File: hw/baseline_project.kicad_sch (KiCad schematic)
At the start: 20 parts, among them J101 EXT_3V3, Q101 IRLD024PBF, SW101 UP, SW102 DOWN, SW103 LEFT, SW104 RIGHT, SW105 MODE, U101 EK-TM4C123GXL, U102 ESP8266-1, U103 Adafruit ST7735R

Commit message: WIP hardware diagram
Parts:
- added D1: LED, ECE445L:LED_D5.0mm, symbol ECE 445L:LED
- added D2: 1N914, Diode_THT:D_DO-35_SOD27_P7.62mm_Horizontal, symbol Diode:1N914
- added LS1: Speaker, symbol Device:Speaker
- added Q1: IRLD024PBF, ECE445L:DIP920W60P254L490H457Q4N, symbol ECE 445L:IRLD024PBF
- added R1: 330, symbol Device:R_US
- added R2: 10K, symbol Device:R_US
- added R3: 0-2k, ECE445L:Potentiometer, symbol ECE 445L:Potentiometer
- added R4: 1k, symbol Device:R_US
- added R5: 10k, symbol Device:R_US
- added SW1, SW2, SW3, SW4, SW5: UP, ECE445L:SW_PUSH_6mm, symbol ECE 445L:SW_Push
- added U1: HiLetGo_ST7735R, ECE445L:hiletgo_st7735r, symbol ECE 445L:HiLetGo_ST7735R
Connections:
- net +3V3: now also D2.1 (K), LS1.1, R2.1, R4.1, U1.15 (LED+), U1.2 (VCC)
- net GND: now also D1.1 (K), Q1.4 (S), R3.3, SW1.1, U1.1 (GND), U1.16 (LED-)
- net PC6: now also R2.2, SW1.2
- net PE1: now also R3.1, R4.2
- net PE2: now also R1.1
- net PF1: now also R5.1
- new net: D2.2 (A), LS1.2, Q1.1 (D), Q1.2 (D)
- new net: Q1.3 (G), R5.2
- new net: D1.2 (A), R1.2
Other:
- note added: "Lab 1 Schematics"
- note added: "Lab 2 Schematics"
- note added: "Lab 3 Schematics"
- note added: "Negative Logic"
- note added: "Positive Logic"

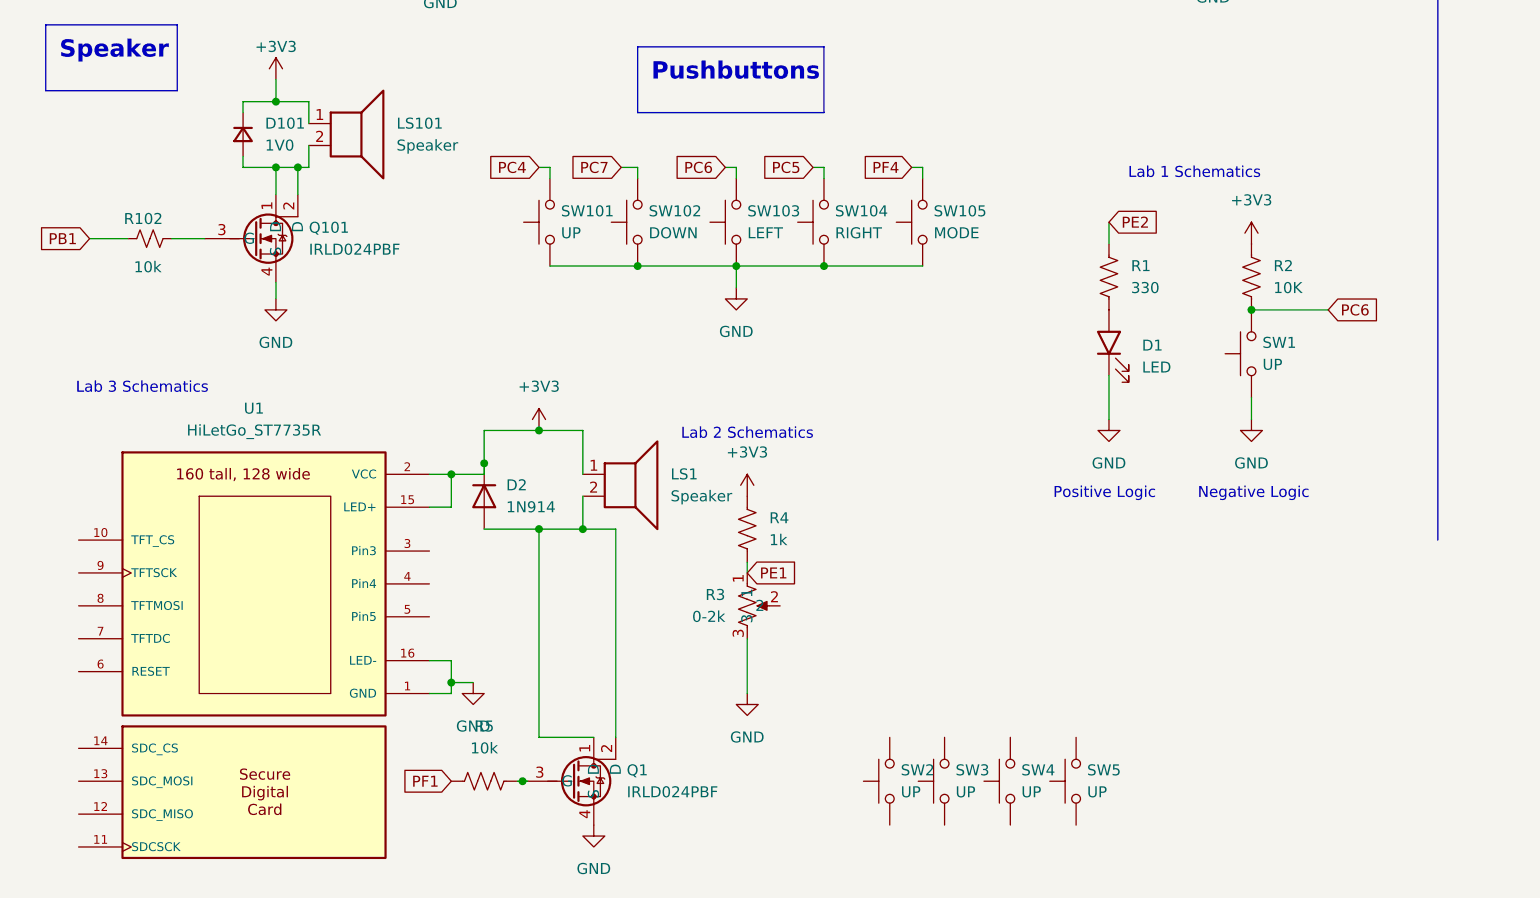
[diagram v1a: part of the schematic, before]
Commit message: HW done for current specs, completed some of prep deliverables
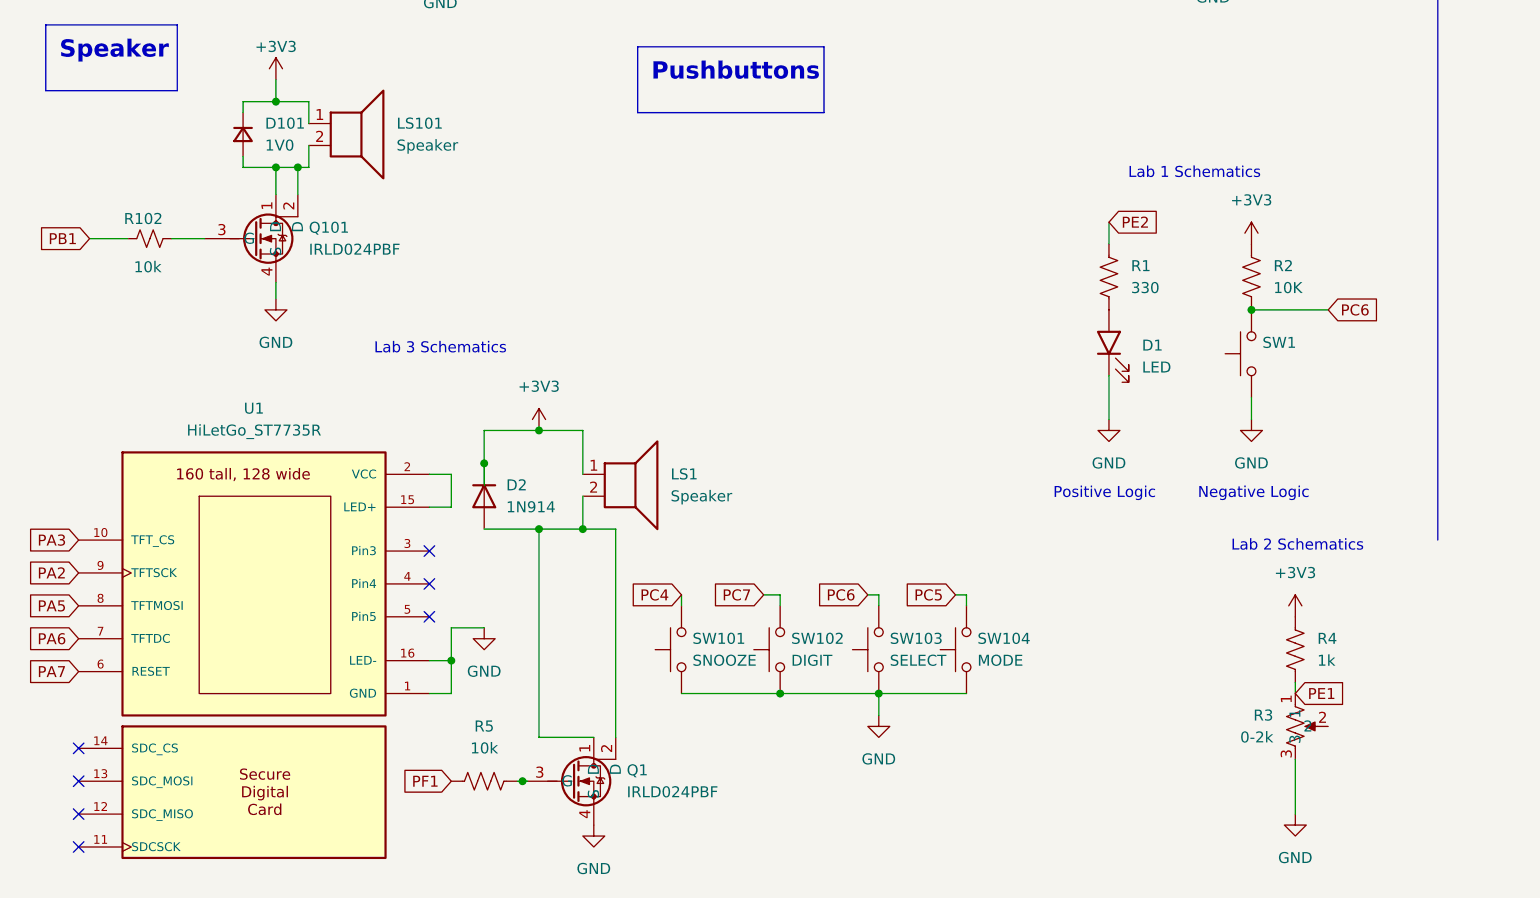
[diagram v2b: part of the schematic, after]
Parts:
- removed SW105: MODE, Button_Switch_THT:SW_PUSH_6mm, symbol Switch:SW_Push
- removed SW2, SW3, SW4, SW5: UP, ECE445L:SW_PUSH_6mm, symbol ECE 445L:SW_Push
- SW101: value UP -> SNOOZE
- SW102: value DOWN -> DIGIT
- SW103: value LEFT -> SELECT
- SW104: value RIGHT -> MODE
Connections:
- net +3V3: no longer U1.15 (LED+), U1.2 (VCC)
- net PA2: now also U1.9 (TFTSCK)
- net PA3: now also U1.10 (TFT_CS)
- net PA5: now also U1.8 (TFTMOSI)
- net PA6: now also U1.7 (TFTDC)
- net PA7: now also U1.6 (RESET)
- new net: U1.15 (LED+), U1.2 (VCC)
- no-connect marks 1 -> 8
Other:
- moved on the sheet: R3, R4, SW101, SW102, SW103, SW104
